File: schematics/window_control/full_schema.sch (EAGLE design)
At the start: 86 parts, among them IC1 MEGA32-P, J1 SERVO, Q10 2N3906BU, Q11 2N3904, Q12 2N3906BU, Q13 2N3904, Q14 2N3904, Q16 2N3906BU, Q17 STP14NM50N, Q4 2N3904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

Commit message: actualized schematics of outdoor noise sensor module
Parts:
- removed C11: C-1, my_devices:C-1
- removed C12, C13: 1000 uF, my_devices:C
- removed C14: 10 uF, my_devices:C
- removed C15, C7: 3 nF ?, my_devices:C-1
- removed C8: 0.01 uF, my_devices:C-1
- removed D2: DB104, my_devices:DIODE_BRIDGE
- removed D3, D4, D6: SB560, my_devices:D_SCHOTTKY
- removed D5: BAT41, my_devices:D_SCHOTTKY
- removed L1: ~6 uH, my_devices:L-4
- removed L2: L, my_devices:L
- removed L3: 1000 uH, my_devices:L
- removed Q10, Q12: 2N3906BU, my_devices:TRANSISTOR_PNP
- removed Q11, Q13, Q14: 2N3904, my_devices:TRANSISTOR_NPN
- removed Q8, Q9: STP14NM50N, my_devices:MOSFET_N
- removed SW2: SWITCH, my_devices:SWITCH
- removed U2: CD4047, my_devices:CD4047
- removed U5: KIA7805API-U/PF, my_devices:VOLTAGE_REGULATOR
- added J2, J3, J4, J5: J2, my_devices:J2
- added Q2: 2N3904, my_devices:TRANSISTOR_NPN
- added R21: RD, my_devices:RD
- C1: value 100 pF -> 0.22 uF; device my_devices:C-1 -> my_devices:C
- C4: value 1000 uF -> 4.7 nF; device my_devices:C -> my_devices:C-1
- R13: value 10K -> 200K; device my_devices:RD -> my_devices:R
- R15: value 5K / 125 mW -> 200K
- R3: value 2,2 K -> 10K
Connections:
- removed net +5V_GEN: C4.PIN_PLUS, D6.P$1, L3.P$1, SW2.P$2, U2.-TRG, U2.AST, U2.AST_, U2.VCC
- removed net N$14: C11.P$2, D2.AC1, L2.P$2
- removed net N$15: C11.P$1, D2.AC2, L2.P$1
- removed net N$21: BM1.P$2, C8.P$2, R3.P$1
- removed net N$25: C7.P$2, D3.P$1, L1.P$1
- removed net N$27: C15.P$2, C7.P$1, D6.P$2, L1.P$2
- removed net N$30: C14.PIN_PLUS, D5.P$2, Q11.C, Q13.C, R15.P$2
- removed net N$31: C15.P$1, D4.P$1, L1.P$3
- removed net N$33: Q12.E, Q13.E, Q9.G
- removed net N$34: R13.P1, U2.R
- removed net N$4: D4.P$2, Q9.D
- removed net N$41: Q10.B, Q11.B, U2.Q_
- removed net N$42: Q12.B, Q13.B, U2.Q
- removed net N$45: Q14.B, U2.OSC_OUT
- net +5V: now also J2.PIN_2; no longer SW2.P$1
- net GND: now also J2.PIN_1; no longer C14.PIN_GND, C4.PIN_GND, Q10.C, Q12.C, Q14.E, Q8.S, Q9.S, R15.P$1, U2.+TRG, U2.EXT_RESET, U2.GND, U2.RE_TRG
- net N$10: now also J3.PIN_2, J4.PIN_1; no longer C1.P$1, R13.P2, R13.P3, U2.RC
- net N$11: now also BM1.P$2, C1.PIN_PLUS, R3.P$2; no longer C1.P$2, U2.C
- net N$12: now also C1.PIN_GND, Q2.B, R13.P$1, R15.P$2; no longer Q10.E, Q11.E, Q8.G
- net N$13: now also C4.P$1, Q2.C, R21.P2, R21.P3; no longer D3.P$2, Q8.D
- net N$19: now also C4.P$2; no longer C8.P$1
- net N$9: now also J3.PIN_1, J4.PIN_2; no longer D5.P$1, L3.P$2, Q14.C
- net OUTDOOR_+5V: now also J5.PIN_1, R13.P$2, R21.P1, R3.P$1; no longer C13.PIN_PLUS, R3.P$2, U5.OUT
- net OUTDOOR_GND: now also J5.PIN_2, Q2.E, R15.P$1; no longer C12.PIN_GND, C13.PIN_GND, D2.GND, U5.GND
- net VCC: no longer C12.PIN_PLUS, D2.VCC, U5.IN
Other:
- note added: "Indoor modules"
- note added: "Outdoor module"
- note removed: "=> WINDOW =>"
- note removed: "Freq ~ Q: 225 KHz OSC OUT: 450 KHz"
- note removed: "calc L -> https://coil32.ru/calc/ferrite-rod.html"
- note removed: "calc LC -> https://coil32.ru/calc/jslcc.html"
- note removed: "https://vip-cxema.org/index.php/online-raschjoty/366-raschjot-povyshayushchego-dc-dc-preobrazovatelya"
- note removed: "~15-20V max 50 mA"
- moved on the sheet: BM1, C10, C2, C3, C5, C6, C9, IC1, R14, R15, R18, R3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

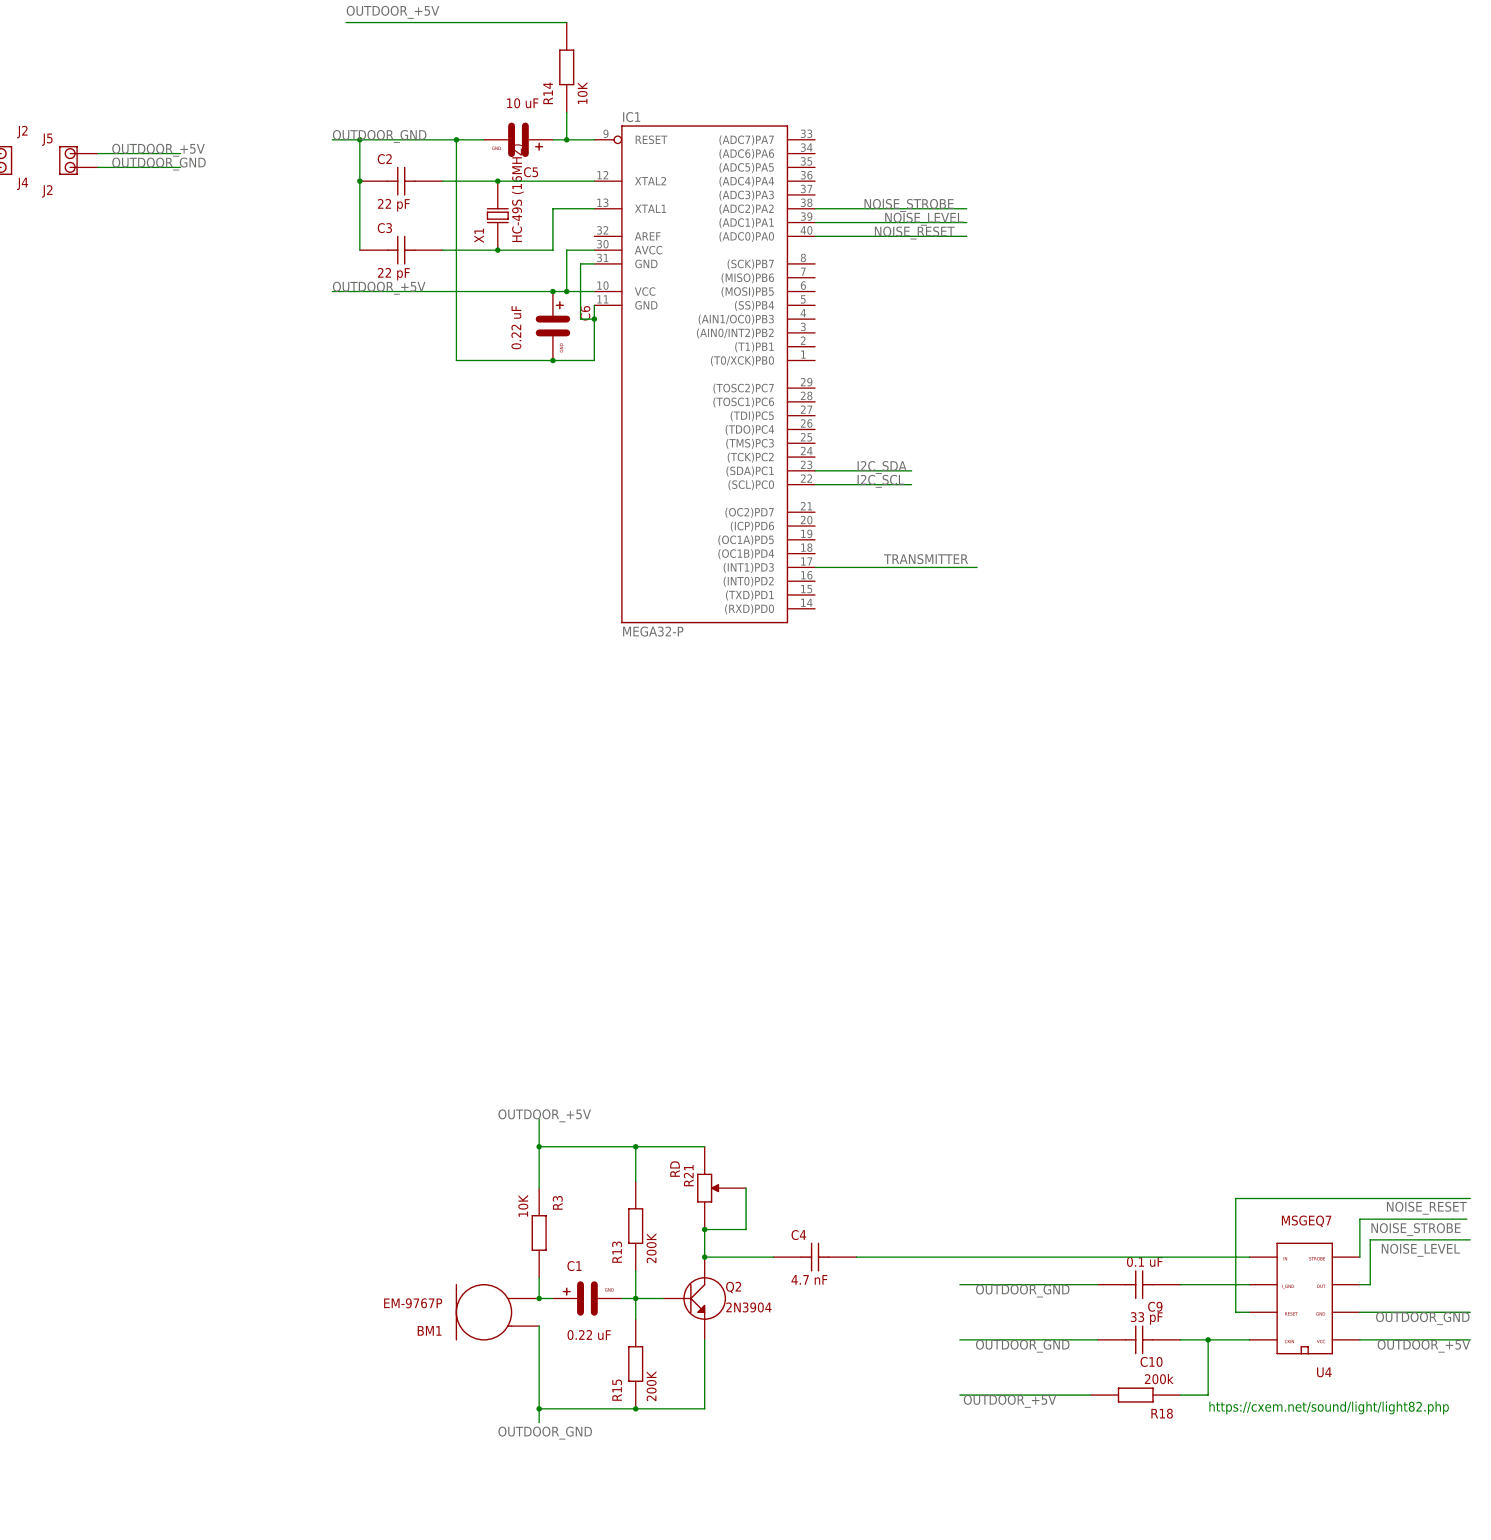
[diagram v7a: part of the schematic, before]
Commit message: actualized schematics of outdoor noise sensor module
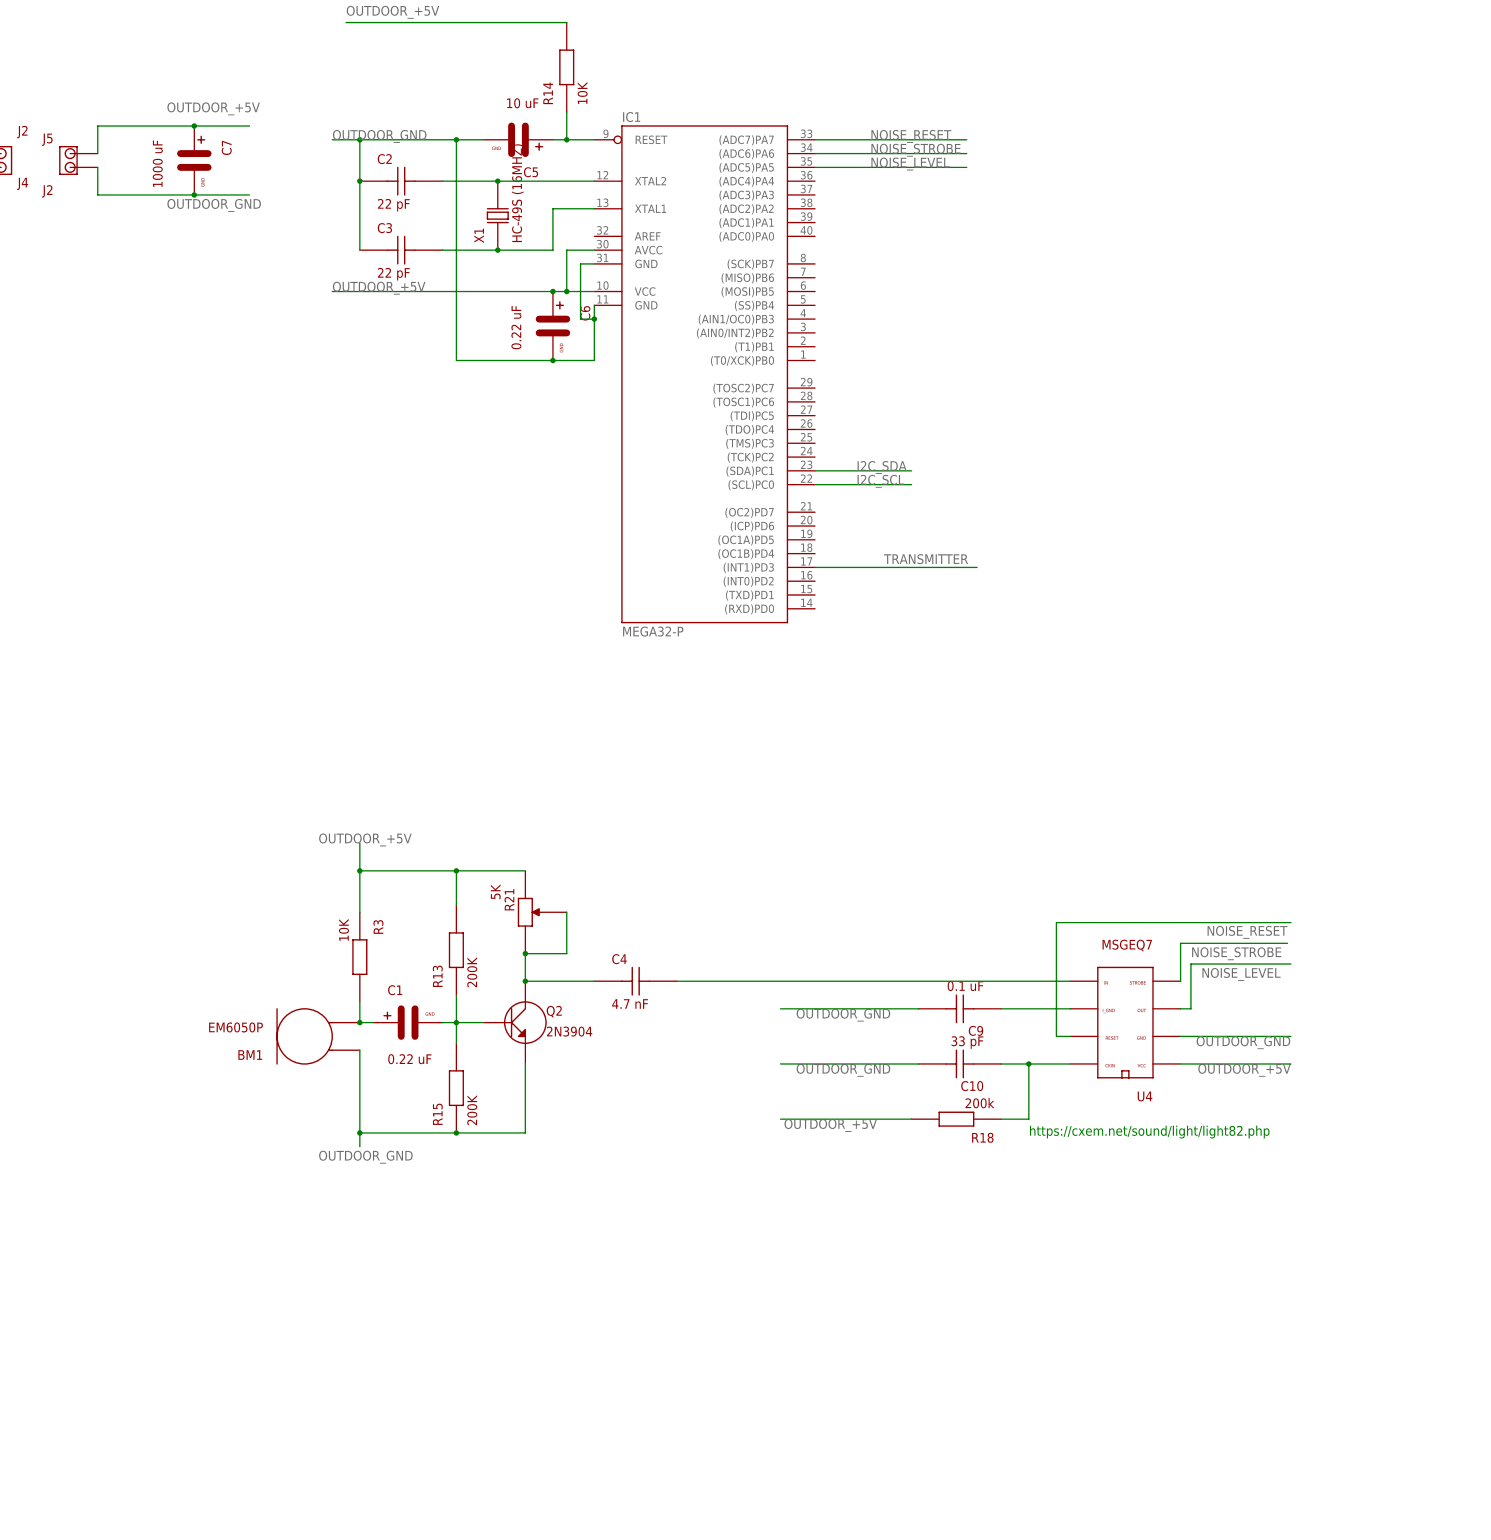
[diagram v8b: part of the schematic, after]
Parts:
- added C7: 1000 uF, my_devices:C
- BM1: value EM-9767P -> EM6050P
- R21: value RD -> 5K
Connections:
- net NOISE_LEVEL: now also IC1.(ADC5)PA5; no longer IC1.(ADC1)PA1
- net NOISE_RESET: now also IC1.(ADC7)PA7; no longer IC1.(ADC0)PA0
- net NOISE_STROBE: now also IC1.(ADC6)PA6; no longer IC1.(ADC2)PA2
- net OUTDOOR_+5V: now also C7.PIN_PLUS
- net OUTDOOR_GND: now also C7.PIN_GND
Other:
- moved on the sheet: BM1, C1, C10, C4, C9, Q2, R13, R15, R18, R21, R3, U4
